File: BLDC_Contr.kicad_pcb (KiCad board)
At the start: 4 copper layers, 90 x 65 mm, 100 parts, among them J1 XT60, J10 PH, J2 Conn_ARM_SWD_TagConnect_TC2030, J3 PH, J4 PH, J5 PH, J6 PH, J7 PH, J8 PIN, Q1 CSD18540Q5B, Q2 CSD18540Q5B, Q3 CSD18540Q5B, Q4 CSD18540Q5B, Q5 CSD18540Q5B, Q6 CSD18540Q5B, U1 STM32G431CBU6, U2 DRV8323RSRGZR, U3 AMS1117-3.3, Y1 Crystal_16Mhz

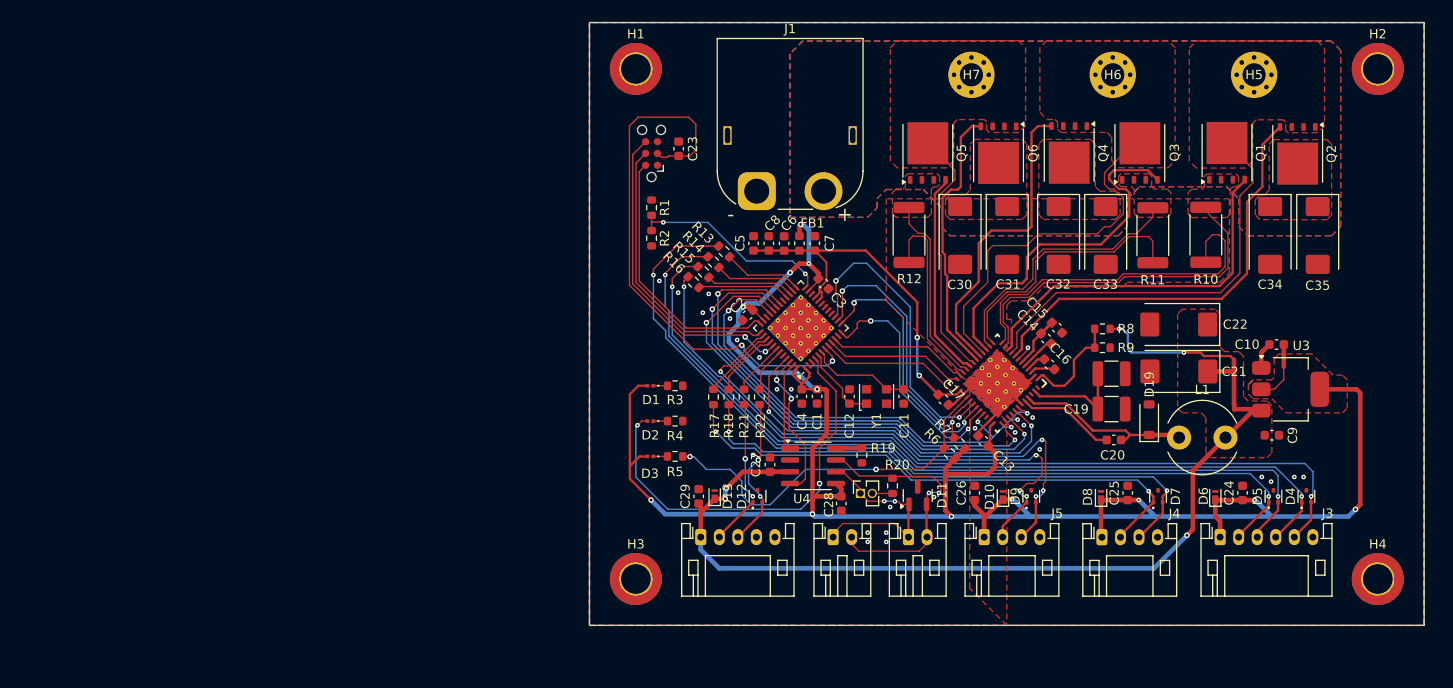
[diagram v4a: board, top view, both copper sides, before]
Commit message: changed most 0603 parts to 0402. wiring changed. pcb dimesion from 65*80mm to 60*80mm
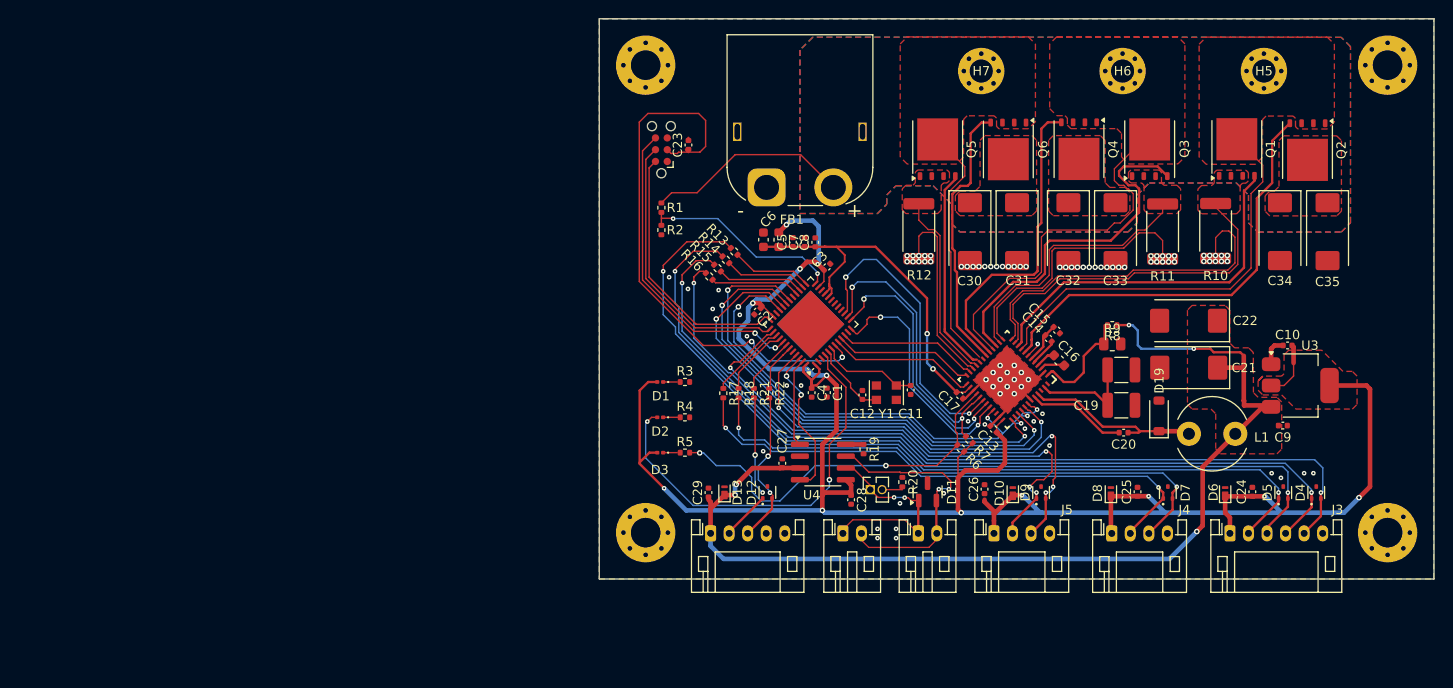
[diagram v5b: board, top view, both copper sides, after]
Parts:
- C1, C10, C11, C12, C13, C14, C15, C17, C2, C20, C23, C24, C25, C26, C27, C28, C29, C3, C4, C5, C7, C8, C9: footprint Capacitor_SMD:C_0603_1608Metric -> Capacitor_SMD:C_0402_1005Metric
- H1, H2, H3, H4: footprint MountingHole:MountingHole_3.2mm_M3_DIN965_Pad_TopBottom -> MountingHole:MountingHole_3.2mm_M3_Pad_Via
- R1, R13, R14, R15, R16, R17, R18, R19, R2, R20, R21, R22, R3, R4, R5, R6, R7, R8: footprint Resistor_SMD:R_0603_1608Metric -> Resistor_SMD:R_0402_1005Metric
- R9: footprint Resistor_SMD:R_0603_1608Metric -> Resistor_SMD:R_0805_2012Metric
- moved H4 5.11 mm to (171.1, 80.0)
- moved H3 5.11 mm to (91.1, 80.0)
- moved C8 5.01 mm to (109.3, 48.7)
- moved C5 4.25 mm to (106.9, 48.7)
- moved C6 2.27 mm to (103.8, 48.4)
- moved FB1 2.27 mm to (105.4, 48.4)
- moved C3 1.84 mm to (110.6, 51.4), turned to 45 degrees
- moved C17 1.83 mm to (124.9, 65.2)
- moved R16 1.80 mm to (97.9, 52.4)
- moved C13 1.68 mm to (128.6, 68.8)
- moved R15 1.58 mm to (98.8, 51.5)
- moved C9 1.58 mm to (159.8, 68.5)
- moved C12 1.40 mm to (114.4, 65.2)
- moved R2 1.38 mm to (92.8, 47.4)
- moved R14 1.36 mm to (99.7, 50.6)
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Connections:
- net /SPI1_MISO_C renamed /SPI2_MISO_C
- net /SPI1_MOSI_C renamed /SPI2_SCK_C
- net /SPI1_NCS_C renamed /SPI2_NCS_C
- net /SPI1_SCK_C renamed /SPI2_MOSI_C
- H1 pad 1: (no net) -> GND
- H2 pad 1: (no net) -> GND
- H3 pad 1: (no net) -> GND
- H4 pad 1: (no net) -> GND
- R14 pad 1: SP2_MOSI -> SP2_SCK
- R16 pad 2: SP2_SCK -> SP2_MOSI
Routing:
- net +BATT: track 20.7 -> 40.1 mm
- net GND: track 107.6 -> 99.8 mm, vias 26 -> 93
- net +3.3V: track 234.4 -> 235.8 mm
- net /SPI2_MOSI_C: track 88.7 -> 89.7 mm
- net USER_LED: track 44.9 -> 43.9 mm
- net /SPI2_MISO_C: track 90.5 -> 91.5 mm
- net Net-(U4-S): track 2.82 -> 1.92 mm
- net /VCP: track 3.86 -> 2.99 mm
- net /SPI2_SCK_C: track 91.8 -> 92.6 mm
- net /SPI2_NCS_C: track 94.1 -> 94.7 mm
- net SHB: track 40.0 -> 39.5 mm
- net +5V: track 116.0 -> 115.5 mm
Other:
- board size 90 x 65 mm -> 90 x 60.4 mm

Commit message: DRCing not done
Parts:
- H1, H2, H3, H4: footprint MountingHole:MountingHole_3.2mm_M3_Pad_Via -> MountingHole:MountingHole_3.2mm_M3_Pad_TopBottom
- H5: value MountingHole_Pad_MP -> A; footprint MountingHole:MountingHole_2.5mm_Pad_Via -> MountingHole:MountingHole_2.5mm_Pad_TopBottom
- H6: value MountingHole_Pad_MP -> B; footprint MountingHole:MountingHole_2.5mm_Pad_Via -> MountingHole:MountingHole_2.5mm_Pad_TopBottom
- H7: value MountingHole_Pad_MP -> C; footprint MountingHole:MountingHole_2.5mm_Pad_Via -> MountingHole:MountingHole_2.5mm_Pad_TopBottom
- moved R20 0.56 mm to (118.5, 74.0)
- moved C26 0.50 mm to (128.0, 75.6)
- moved C1 0.47 mm to (110.2, 64.6)
- moved C4 0.29 mm to (109.0, 64.6)
- moved C28 0.29 mm to (113.2, 76.2)
- moved C29 0.24 mm to (97.8, 75.4)
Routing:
- net SHC: track 26.8 -> 0.00 mm, vias 0 -> 62
- net GLC: track 21.9 -> 0.00 mm
- net +3.3V: track 235.8 -> 254.3 mm, vias 12 -> 13
- net AMT_A: track 5.74 -> 0.00 mm
- net AMT_B: track 4.80 -> 0.00 mm
- net /AMT_A_C: track 15.6 -> 16.2 mm
- net SPB: track 29.4 -> 29.1 mm, vias 0 -> 16
- net SPC: vias 0 -> 16
- net SPA: vias 0 -> 16
- net SHB: vias 0 -> 62
- net SHA: vias 0 -> 62
- net GND: vias 93 -> 125
- net +BATT: vias 1 -> 163
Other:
- outline, holes or cut-outs redrawn

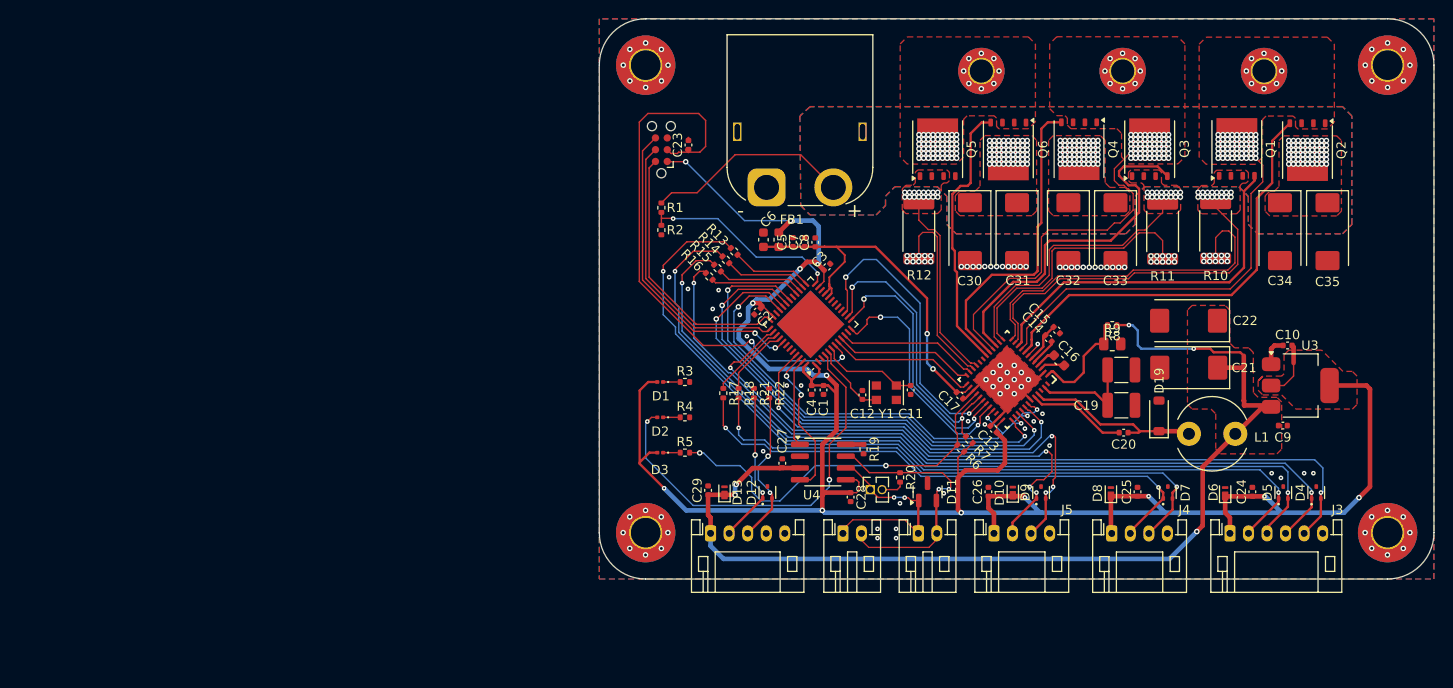
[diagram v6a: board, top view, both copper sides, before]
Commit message: changed most 0603 parts to 0402. wiring changed. pcb dimesion from 65*80mm to 60*80m
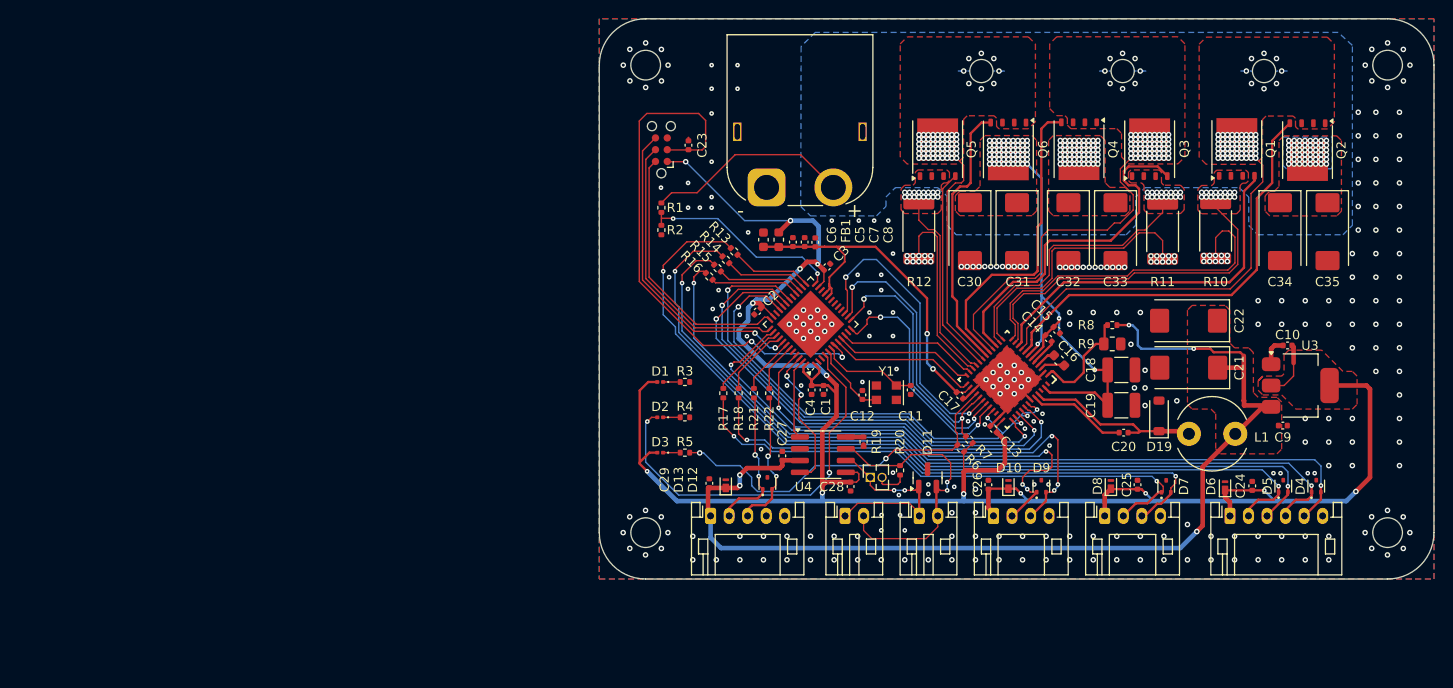
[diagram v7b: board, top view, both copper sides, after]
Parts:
- H1, H2, H3, H4: footprint MountingHole:MountingHole_3.2mm_M3_Pad_TopBottom -> MountingHole:MountingHole_3.2mm_M3
- H5: value A -> MountingHole_Pad_MP; footprint MountingHole:MountingHole_2.5mm_Pad_TopBottom -> MountingHole:MountingHole_2.5mm
- H6: value B -> MountingHole_Pad_MP; footprint MountingHole:MountingHole_2.5mm_Pad_TopBottom -> MountingHole:MountingHole_2.5mm
- H7: value C -> MountingHole_Pad_MP; footprint MountingHole:MountingHole_2.5mm_Pad_TopBottom -> MountingHole:MountingHole_2.5mm
- moved J4 2.04 mm to (140.6, 78.2)
- moved J7 1.89 mm to (112.6, 78.2)
- moved J6 1.88 mm to (120.6, 78.2)
- moved J5 1.88 mm to (128.6, 78.2)
- moved J10 1.88 mm to (98.1, 78.2)
- moved J3 1.88 mm to (154.1, 78.2)
- moved D11 1.51 mm to (121.5, 74.1)
- moved J8 1.32 mm to (115.3, 74.0)
- moved C28 1.14 mm to (113.2, 75.0)
- moved D12 0.98 mm to (104.2, 74.7)
- moved D10 0.86 mm to (130.2, 75.0)
- moved C27 0.80 mm to (105.8, 71.7)
- moved R19 0.80 mm to (114.6, 70.2)
- moved U4 0.80 mm to (110.2, 71.6)
- moved C29 0.77 mm to (97.9, 74.7)
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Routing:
- net +BATT: track 40.1 -> 73.3 mm, vias 163 -> 159
- net SHC: track 0.00 -> 24.7 mm
- net GLC: track 0.00 -> 22.3 mm
- net +3.3V: track 254.3 -> 241.3 mm
- net AMT_A: track 0.00 -> 6.12 mm
- net AMT_B: track 0.00 -> 5.23 mm
- net /CAN_H_C: track 29.5 -> 32.1 mm
- net /SPI2_SCK_C: track 92.6 -> 90.7 mm
- net /SPI2_MOSI_C: track 89.7 -> 88.0 mm
- net /AMT_B_C: track 16.6 -> 15.1 mm
- net I2C_SDA: track 50.8 -> 49.4 mm
- net USER_LED: track 43.9 -> 42.6 mm
- net SHB: track 39.5 -> 38.2 mm
- net NFAULT_PRE: track 40.6 -> 39.4 mm
- net /CAN_L_C: track 23.3 -> 22.3 mm
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- added copper zone on B.Cu, net SHA
- added copper zone on B.Cu, net SHB
- added copper zone on B.Cu, net SHC
- added copper zone on In2.Cu, net SPA
- added copper zone on In2.Cu, net SPB
- added copper zone on In2.Cu, net SPC
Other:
- board text added: "J5"
